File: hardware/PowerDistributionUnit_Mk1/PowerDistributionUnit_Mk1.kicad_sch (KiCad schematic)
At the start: 33 parts, among them J1 XT-30, J2 Molex_NanoFit_2x8, J3 Molex_NanoFit_1x6, J4 Molex_NanoFit_1x2, J5 Molex_NanoFit_1x2, J8 Molex_NanoFit_1x2, J9 Molex_NanoFit_1x2

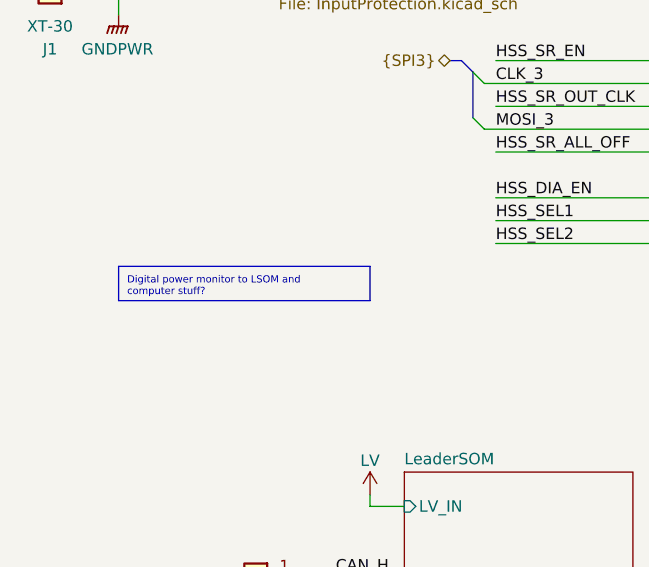
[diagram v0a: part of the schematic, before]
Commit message: update schematic documentation, clean up, update titleblocks
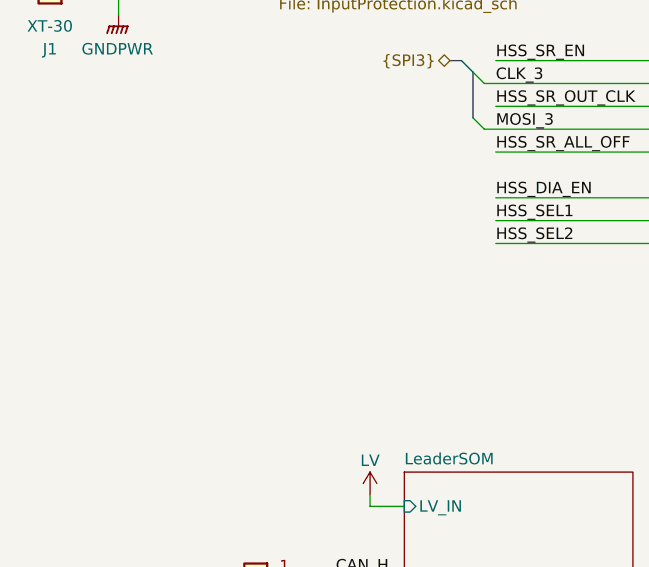
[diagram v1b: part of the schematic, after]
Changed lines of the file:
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@@
 	(title_block
 		(title "Big Brain Power Distribution Unit (Mk.1)")
-		(rev "0")
+		(date "2026-02-28")
+		(rev "B")
 		(company "Longhorn Racing Solar")
 		(comment 1 "Changxu Liu")
@@
 			)
 			(justify left top)
-		)
-	)
-	(text_box "Digital power monitor to LSOM and computer stuff?"
-		(exclude_from_sim no)
-		(at 27.94 62.23 0)
-		(size 27.94 3.81)
-		(margins 0.9525 0.9525 0.9525 0.9525)
-		(stroke
-			(width 0)
-			(type solid)
-			(color 255 0 0 1)
-		)
-		(fill
-			(type none)
-		)
-		(effects
-			(font
-				(size 0.8 0.8)
-				(color 255 0 0 1)
-			)
-			(justify left top)

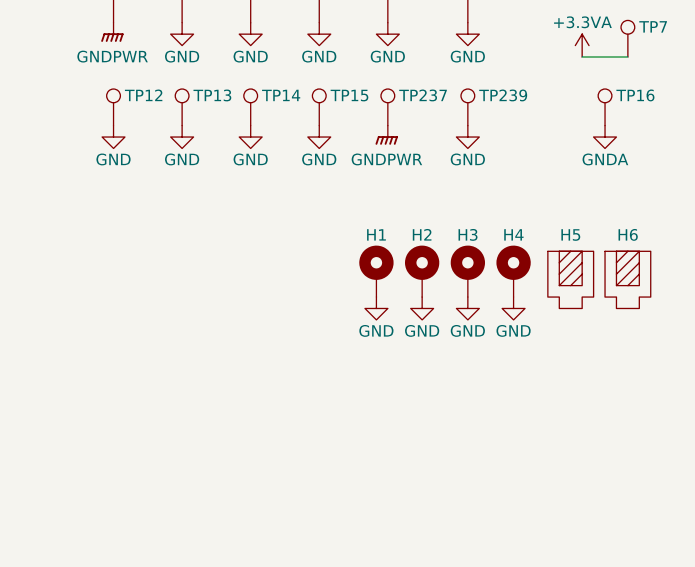
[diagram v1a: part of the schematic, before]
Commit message: add center mounting hole
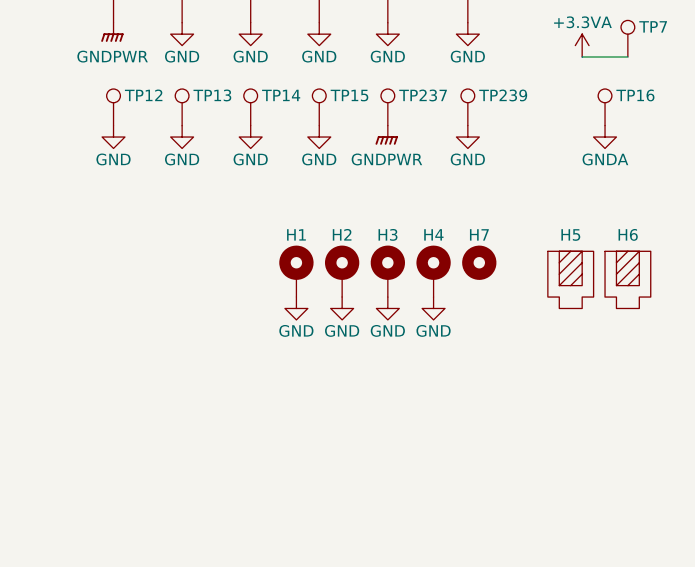
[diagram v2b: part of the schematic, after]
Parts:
- added H7: MountingHole, MountingHole:MountingHole_3.2mm_M3, symbol Mechanical:MountingHole
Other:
- moved on the sheet: H1, H2, H3, H4
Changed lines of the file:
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@@
 	(symbol
 		(lib_id "power:GND")
-		(at 251.46 156.21 0)
+		(at 242.57 156.21 0)
 		(unit 1)
 		(exclude_from_sim no)
@@
 		(dnp no)
 		(property "Reference" "#PWR0481"
-			(at 251.46 162.56 0)
+			(at 242.57 162.56 0)
 			(effects
 				(font
@@
 		)
 		(property "Value" "GND"
-			(at 251.46 160.02 0)
+			(at 242.57 160.02 0)
 			(effects
 				(font
@@
 		)
 		(property "Footprint" ""
-			(at 251.46 156.21 0)
+			(at 242.57 156.21 0)
 			(effects
 				(font
@@
 		)
 		(property "Datasheet" ""
-			(at 251.46 156.21 0)
+			(at 242.57 156.21 0)
 			(effects
 				(font
@@
 		)
 		(property "Description" "Power symbol creates a global label with name \"GND\" , ground"
-			(at 251.46 156.21 0)
+			(at 242.57 156.21 0)
 			(effects
 				(font
@@
 	(symbol
 		(lib_id "power:GND")
-		(at 256.54 156.21 0)
+		(at 247.65 156.21 0)
 		(unit 1)
 		(exclude_from_sim no)
@@
 		(dnp no)
 		(property "Reference" "#PWR0482"
-			(at 256.54 162.56 0)
+			(at 247.65 162.56 0)
 			(effects
 				(font
@@
 		)
 		(property "Value" "GND"
-			(at 256.54 160.02 0)
+			(at 247.65 160.02 0)
 			(effects
 				(font
@@
 		)
 		(property "Footprint" ""
-			(at 256.54 156.21 0)
+			(at 247.65 156.21 0)
 			(effects
 				(font
@@
 		)
 		(property "Datasheet" ""
-			(at 256.54 156.21 0)
+			(at 247.65 156.21 0)
 			(effects
 				(font
@@
 		)
 		(property "Description" "Power symbol creates a global label with name \"GND\" , ground"
-			(at 256.54 156.21 0)
+			(at 247.65 156.21 0)
 			(effects
 				(font
@@
 				(path "/6abaf095-8ba7-4306-8425-59a9eb37aa2b"
 					(reference "#PWR0482")
+					(unit 1)
+				)
+			)
+		)
+	)
+	(symbol
+		(lib_id "Mechanical:MountingHole")
+		(at 257.81 152.4 0)
+		(unit 1)
+		(exclude_from_sim no)
+		(in_bom no)
+		(on_board yes)
+		(dnp no)
+		(property "Reference" "H7"
+			(at 257.81 149.352 0)
+			(effects
+				(font
+					(size 1.27 1.27)
+				)
+			)
+		)
+		(property "Value" "MountingHole"
+			(at 260.35 152.3999 0)
+			(effects
+				(font
+					(size 1.27 1.27)
+				)
+				(justify left)
+				(hide yes)
+			)
+		)
+		(property "Footprint" "MountingHole:MountingHole_3.2mm_M3"
+			(at 257.81 152.4 0)
+			(effects
+				(font
+					(size 1.27 1.27)
+				)
+				(hide yes)
+			)
+		)
+		(property "Datasheet" "~"
+			(at 257.81 152.4 0)
+			(effects
+				(font
+					(size 1.27 1.27)
+				)
+				(hide yes)
+			)
+		)
+		(property "Description" "Mounting Hole without connection"
+			(at 257.81 152.4 0)
+			(effects
+				(font
+					(size 1.27 1.27)
+				)
+				(hide yes)
+			)
+		)
+		(instances
+			(project "PowerDistributionUnit_Mk1"
+				(path "/6abaf095-8ba7-4306-8425-59a9eb37aa2b"
+					(reference "H7")
 					(unit 1)
 				)
@@
 	(symbol
 		(lib_id "power:GND")
-		(at 261.62 156.21 0)
+		(at 252.73 156.21 0)
 		(unit 1)
 		(exclude_from_sim no)
@@
 		(dnp no)
 		(property "Reference" "#PWR0483"
-			(at 261.62 162.56 0)
+			(at 252.73 162.56 0)
 			(effects
 				(font
@@
 		)
 		(property "Value" "GND"
-			(at 261.62 160.02 0)
+			(at 252.73 160.02 0)
 			(effects
 				(font
@@
 		)
 		(property "Footprint" ""
-			(at 261.62 156.21 0)
+			(at 252.73 156.21 0)
 			(effects
 				(font
@@
 		)
 		(property "Datasheet" ""
-			(at 261.62 156.21 0)
+			(at 252.73 156.21 0)
 			(effects
 				(font
@@
 		)
 		(property "Description" "Power symbol creates a global label with name \"GND\" , ground"
-			(at 261.62 156.21 0)
+			(at 252.73 156.21 0)
 			(effects
 				(font
@@
 	(symbol
 		(lib_id "Mechanical:MountingHole_Pad")
-		(at 251.46 153.67 0)
+		(at 242.57 153.67 0)
 		(unit 1)
 		(exclude_from_sim no)
@@
 		(dnp no)
 		(property "Reference" "H2"
-			(at 251.46 149.352 0)
+			(at 242.57 149.352 0)
 			(effects
 				(font
@@
 		)
 		(property "Value" "MountingHole_Pad"
-			(at 254 153.6699 0)
+			(at 245.11 153.6699 0)
 			(effects
 				(font
@@
 		)
 		(property "Footprint" "MountingHole:MountingHole_3.2mm_M3_Pad"
-			(at 251.46 153.67 0)
+			(at 242.57 153.67 0)
 			(effects
 				(font
@@
 		)
 		(property "Datasheet" "~"
-			(at 251.46 153.67 0)
+			(at 242.57 153.67 0)
 			(effects
 				(font
@@
 		)
 		(property "Description" "Mounting Hole with connection"
-			(at 251.46 153.67 0)
+			(at 242.57 153.67 0)
 			(effects
 				(font
@@
 	(symbol
 		(lib_id "Mechanical:MountingHole_Pad")
-		(at 256.54 153.67 0)
+		(at 247.65 153.67 0)
 		(unit 1)
 		(exclude_from_sim no)
@@
 		(dnp no)
 		(property "Reference" "H3"
-			(at 256.54 149.352 0)
+			(at 247.65 149.352 0)
 			(effects
 				(font
@@
 		)
 		(property "Value" "MountingHole_Pad"
-			(at 259.08 153.6699 0)
+			(at 250.19 153.6699 0)
 			(effects
 				(font
@@
 		)
 		(property "Footprint" "MountingHole:MountingHole_3.2mm_M3_Pad"
-			(at 256.54 153.67 0)
+			(at 247.65 153.67 0)
 			(effects
 				(font
@@
 		)
 		(property "Datasheet" "~"
-			(at 256.54 153.67 0)
+			(at 247.65 153.67 0)
 			(effects
 				(font
@@
 		)
 		(property "Description" "Mounting Hole with connection"
-			(at 256.54 153.67 0)
+			(at 247.65 153.67 0)
 			(effects
 				(font
@@
 	(symbol
 		(lib_id "Mechanical:MountingHole_Pad")
-		(at 261.62 153.67 0)
+		(at 252.73 153.67 0)
 		(unit 1)
 		(exclude_from_sim no)
@@
 		(dnp no)
 		(property "Reference" "H4"
-			(at 261.62 149.352 0)
+			(at 252.73 149.352 0)
 			(effects
 				(font
@@
 		)
 		(property "Value" "MountingHole_Pad"
-			(at 264.16 153.6699 0)
+			(at 255.27 153.6699 0)
 			(effects
 				(font
@@
 		)
 		(property "Footprint" "MountingHole:MountingHole_3.2mm_M3_Pad"
-			(at 261.62 153.67 0)
+			(at 252.73 153.67 0)
 			(effects
 				(font
@@
 		)
 		(property "Datasheet" "~"
-			(at 261.62 153.67 0)
+			(at 252.73 153.67 0)
 			(effects
 				(font
@@
 		)
 		(property "Description" "Mounting Hole with connection"
-			(at 261.62 153.67 0)
+			(at 252.73 153.67 0)
 			(effects
 				(font
@@
 	(symbol
 		(lib_id "power:GND")
-		(at 246.38 156.21 0)
+		(at 237.49 156.21 0)
 		(unit 1)
 		(exclude_from_sim no)
@@
 		(dnp no)
 		(property "Reference" "#PWR0480"
-			(at 246.38 162.56 0)
+			(at 237.49 162.56 0)
 			(effects
 				(font
@@
 		)
 		(property "Value" "GND"
-			(at 246.38 160.02 0)
+			(at 237.49 160.02 0)
 			(effects
 				(font
@@
 		)
 		(property "Footprint" ""
-			(at 246.38 156.21 0)
+			(at 237.49 156.21 0)
 			(effects
 				(font
@@
 		)
 		(property "Datasheet" ""
-			(at 246.38 156.21 0)
+			(at 237.49 156.21 0)
 			(effects
 				(font
@@
 		)
 		(property "Description" "Power symbol creates a global label with name \"GND\" , ground"
-			(at 246.38 156.21 0)
+			(at 237.49 156.21 0)
 			(effects
 				(font
@@
 	(symbol
 		(lib_id "Mechanical:MountingHole_Pad")
-		(at 246.38 153.67 0)
+		(at 237.49 153.67 0)
 		(unit 1)
 		(exclude_from_sim no)
@@
 		(dnp no)
 		(property "Reference" "H1"
-			(at 246.38 149.352 0)
+			(at 237.49 149.352 0)
 			(effects
 				(font
@@
 		)
 		(property "Value" "MountingHole_Pad"
-			(at 248.92 153.6699 0)
+			(at 240.03 153.6699 0)
 			(effects
 				(font
@@
 		)
 		(property "Footprint" "MountingHole:MountingHole_3.2mm_M3_Pad"
-			(at 246.38 153.67 0)
+			(at 237.49 153.67 0)
 			(effects
 				(font
@@
 		)
 		(property "Datasheet" "~"
-			(at 246.38 153.67 0)
+			(at 237.49 153.67 0)
 			(effects
 				(font
@@
 		)
 		(property "Description" "Mounting Hole with connection"
-			(at 246.38 153.67 0)
-			(effects
-				(font
+			(at 237.49 153.67 0)
+			(effects
+				(font
